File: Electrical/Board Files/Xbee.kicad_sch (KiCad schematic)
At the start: 0 parts

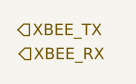
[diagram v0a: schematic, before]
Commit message: Updating for 3v3 operation
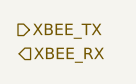
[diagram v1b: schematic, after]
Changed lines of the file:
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@@
 (kicad_sch (version 20211123) (generator eeschema)
   (paper "A4")
-  (hierarchical_label "XBEE_TX" (shape input) (at 170.815 86.741 0)
+  (hierarchical_label "XBEE_TX" (shape output) (at 170.815 86.741 0)
     (effects (font (size 1.27 1.27)) (justify left))
   )

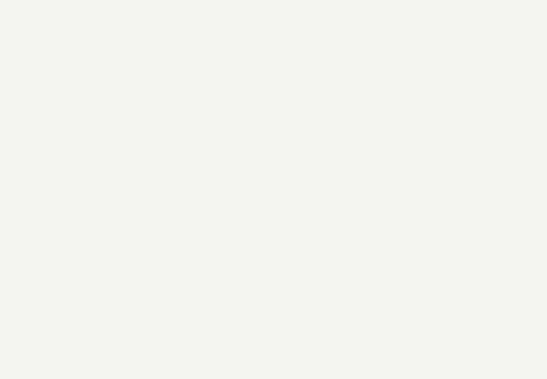
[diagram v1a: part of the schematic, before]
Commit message: Added buzz and vibe, moved SPI, added 2 LEDs
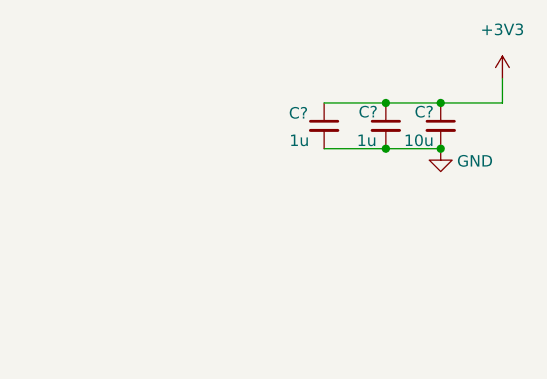
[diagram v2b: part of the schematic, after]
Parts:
- added C?: 10u, symbol Device:C_Small
- added C? (x2): 1u, symbol Device:C_Small
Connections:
- new net +3V3: C?.1, C?.1, C?.1
- new net GND: C?.2, C?.2, C?.2
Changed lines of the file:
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@@
 (kicad_sch (version 20211123) (generator eeschema)
   (paper "A4")
+  (junction (at 219.71 45.212) (diameter 0) (color 0 0 0 0)
+  )
+  (junction (at 213.614 45.212) (diameter 0) (color 0 0 0 0)
+  )
+  (junction (at 219.71 50.292) (diameter 0) (color 0 0 0 0)
+  )
+  (junction (at 213.614 50.292) (diameter 0) (color 0 0 0 0)
+  )
+  (wire (pts (xy 226.568 42.545) (xy 226.568 45.212))
+    (stroke (width 0) (type default) (color 0 0 0 0))
+  )
+  (wire (pts (xy 219.71 45.212) (xy 226.568 45.212))
+    (stroke (width 0) (type default) (color 0 0 0 0))
+  )
+  (wire (pts (xy 219.71 50.292) (xy 213.614 50.292))
+    (stroke (width 0) (type default) (color 0 0 0 0))
+  )
+  (wire (pts (xy 213.614 50.292) (xy 206.756 50.292))
+    (stroke (width 0) (type default) (color 0 0 0 0))
+  )
+  (wire (pts (xy 213.614 45.212) (xy 206.756 45.212))
+    (stroke (width 0) (type default) (color 0 0 0 0))
+  )
+  (wire (pts (xy 219.71 45.212) (xy 213.614 45.212))
+    (stroke (width 0) (type default) (color 0 0 0 0))
+  )
   (hierarchical_label "XBEE_TX" (shape output) (at 170.815 86.741 0)
     (effects (font (size 1.27 1.27)) (justify left))
@@
     (effects (font (size 1.27 1.27)) (justify left))
   )
+  (symbol (lib_id "power:+3V3") (at 226.568 42.545 0) (unit 1)
+    (in_bom yes) (on_board yes) (fields_autoplaced)
+    (property "Reference" "#PWR?" (id 0) (at 226.568 46.355 0)
+      (effects (font (size 1.27 1.27)) hide)
+    )
+    (property "Value" "+3V3" (id 1) (at 226.568 37.084 0))
+    (property "Footprint" "" (id 2) (at 226.568 42.545 0)
+      (effects (font (size 1.27 1.27)) hide)
+    )
+    (property "Datasheet" "" (id 3) (at 226.568 42.545 0)
+      (effects (font (size 1.27 1.27)) hide)
+    )
+    (pin "1")
+  )
+  (symbol (lib_id "Device:C_Small") (at 219.71 47.752 0) (mirror y) (unit 1)
+    (in_bom yes) (on_board yes)
+    (property "Reference" "C?" (id 0) (at 218.948 46.228 0)
+      (effects (font (size 1.27 1.27)) (justify left))
+    )
+    (property "Value" "10u" (id 1) (at 218.948 49.403 0)
+      (effects (font (size 1.27 1.27)) (justify left))
+    )
+    (property "Footprint" "" (id 2) (at 219.71 47.752 0)
+      (effects (font (size 1.27 1.27)) hide)
+    )
+    (property "Datasheet" "~" (id 3) (at 219.71 47.752 0)
+      (effects (font (size 1.27 1.27)) hide)
+    )
+    (pin "1")
+    (pin "2")
+  )
+  (symbol (lib_id "Device:C_Small") (at 213.614 47.752 0) (mirror y) (unit 1)
+    (in_bom yes) (on_board yes)
+    (property "Reference" "C?" (id 0) (at 212.725 46.228 0)
+      (effects (font (size 1.27 1.27)) (justify left))
+    )
+    (property "Value" "1u" (id 1) (at 212.598 49.403 0)
+      (effects (font (size 1.27 1.27)) (justify left))
+    )
+    (property "Footprint" "" (id 2) (at 213.614 47.752 0)
+      (effects (font (size 1.27 1.27)) hide)
+    )
+    (property "Datasheet" "~" (id 3) (at 213.614 47.752 0)
+      (effects (font (size 1.27 1.27)) hide)
+    )
+    (pin "1")
+    (pin "2")
+  )
+  (symbol (lib_id "power:GND") (at 219.71 50.292 0) (unit 1)
+    (in_bom yes) (on_board yes)
+    (property "Reference" "#PWR?" (id 0) (at 219.71 56.642 0)
+      (effects (font (size 1.27 1.27)) hide)
+    )
+    (property "Value" "GND" (id 1) (at 223.52 51.689 0))
+    (property "Footprint" "" (id 2) (at 219.71 50.292 0)
+      (effects (font (size 1.27 1.27)) hide)
+    )
+    (property "Datasheet" "" (id 3) (at 219.71 50.292 0)
+      (effects (font (size 1.27 1.27)) hide)
+    )
+    (pin "1")
+  )
+  (symbol (lib_id "Device:C_Small") (at 206.756 47.752 0) (mirror y) (unit 1)
+    (in_bom yes) (on_board yes)
+    (property "Reference" "C?" (id 0) (at 204.978 46.355 0)
+      (effects (font (size 1.27 1.27)) (justify left))
+    )
+    (property "Value" "1u" (id 1) (at 205.105 49.403 0)
+      (effects (font (size 1.27 1.27)) (justify left))
+    )
+    (property "Footprint" "" (id 2) (at 206.756 47.752 0)
+      (effects (font (size 1.27 1.27)) hide)
+    )
+    (property "Datasheet" "~" (id 3) (at 206.756 47.752 0)
+      (effects (font (size 1.27 1.27)) hide)
+    )
+    (pin "1")
+    (pin "2")
+  )
 )

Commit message: Added Xbee libs and bus aliases
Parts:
- added R21: 10k, symbol Device:R_US
- added U7: XBP9B-DMWTB002, XBP9-DMWTB002-XBEE-PRO-900HP:DIP2200W51P200L3294H279Q20P, symbol xbp9b-dmwtb002:XBP9B-DMWTB002
- gave numbers to parts that had none: 3
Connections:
- net +3V3: now also R21.2, U7.1 (VCC)
- net GND: now also U7.10 (GND)
- new net: R21.1, U7.5 (~{RESET})
- new net XUART.RX: U7.2 (DOUT/DIO13)
- new net XUART.TX: U7.3 (DIN/NCONFIG/DIO14)
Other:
- title: (none) -> Robotics Controller
- moved on the sheet: C33, C34, C35

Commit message: Added hall effect sensors
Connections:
- no-connect marks 0 -> 14
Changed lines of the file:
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@@
   (junction (at 94.234 85.09) (diameter 0) (color 0 0 0 0)
   )
+  (no_connect (at 170.18 80.01))
+  (no_connect (at 170.18 113.03))
+  (no_connect (at 170.18 115.57))
+  (no_connect (at 170.18 118.11))
+  (no_connect (at 170.18 120.65))
+  (no_connect (at 114.3 107.95))
+  (no_connect (at 170.18 85.09))
+  (no_connect (at 170.18 95.25))
+  (no_connect (at 170.18 97.79))
+  (no_connect (at 170.18 100.33))
+  (no_connect (at 170.18 102.87))
+  (no_connect (at 170.18 105.41))
+  (no_connect (at 170.18 107.95))
+  (no_connect (at 170.18 110.49))
   (bus_entry (at 221.869 92.71) (size -2.54 -2.54)
     (stroke (width 0) (type default) (color 0 0 0 0))

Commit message: Updating title block fields and adding pdf schematic
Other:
- company: (none) -> Rockerbotics
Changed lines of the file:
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@@
   (title_block
     (title "Robotics Controller")
+    (date "2022-09-02")
     (rev "A")
+    (company "Rockerbotics")
   )
   (junction (at 100.33 80.01) (diameter 0) (color 0 0 0 0)
